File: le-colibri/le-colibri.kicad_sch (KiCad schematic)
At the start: 61 parts, among them SW1 CPG151101S11, SW10 CPG151101S11, SW11 CPG151101S11, SW12 CPG151101S11, SW13 CPG151101S11, SW14 CPG151101S11, SW15 CPG151101S11, SW16 CPG151101S11, SW17 CPG151101S11, SW18 CPG151101S11, SW19 CPG151101S11, SW2 CPG151101S11, SW20 CPG151101S11, SW21 CPG151101S11, SW22 CPG151101S11, SW23 CPG151101S11, SW24 CPG151101S11, SW25 CPG151101S11, SW26 CPG151101S11, SW27 CPG151101S11, SW28 CPG151101S11, SW29 CPG151101S11, SW3 CPG151101S11, SW30 CPG151101S11, SW4 CPG151101S11, SW5 CPG151101S11, SW6 CPG151101S11, SW7 CPG151101S11, SW8 CPG151101S11, SW9 CPG151101S11, U1 Seeeduino Xiao rp2040

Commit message: "first" "release"
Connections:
- net C1: now also U1.4 (P29)
- net C2: now also U1.5 (P6)
- net C3: now also U1.6 (P7)
- net C4: now also U1.7 (P0)
- net C5: now also U1.14 (P1)
- net R1: now also U1.11 (P3)
- net R2: now also U1.12 (P4)
- net R3: now also U1.13 (P2)
- net R4: now also U1.1 (P26)
- net R5: now also U1.2 (P27)
- net R6: now also U1.3 (P28)

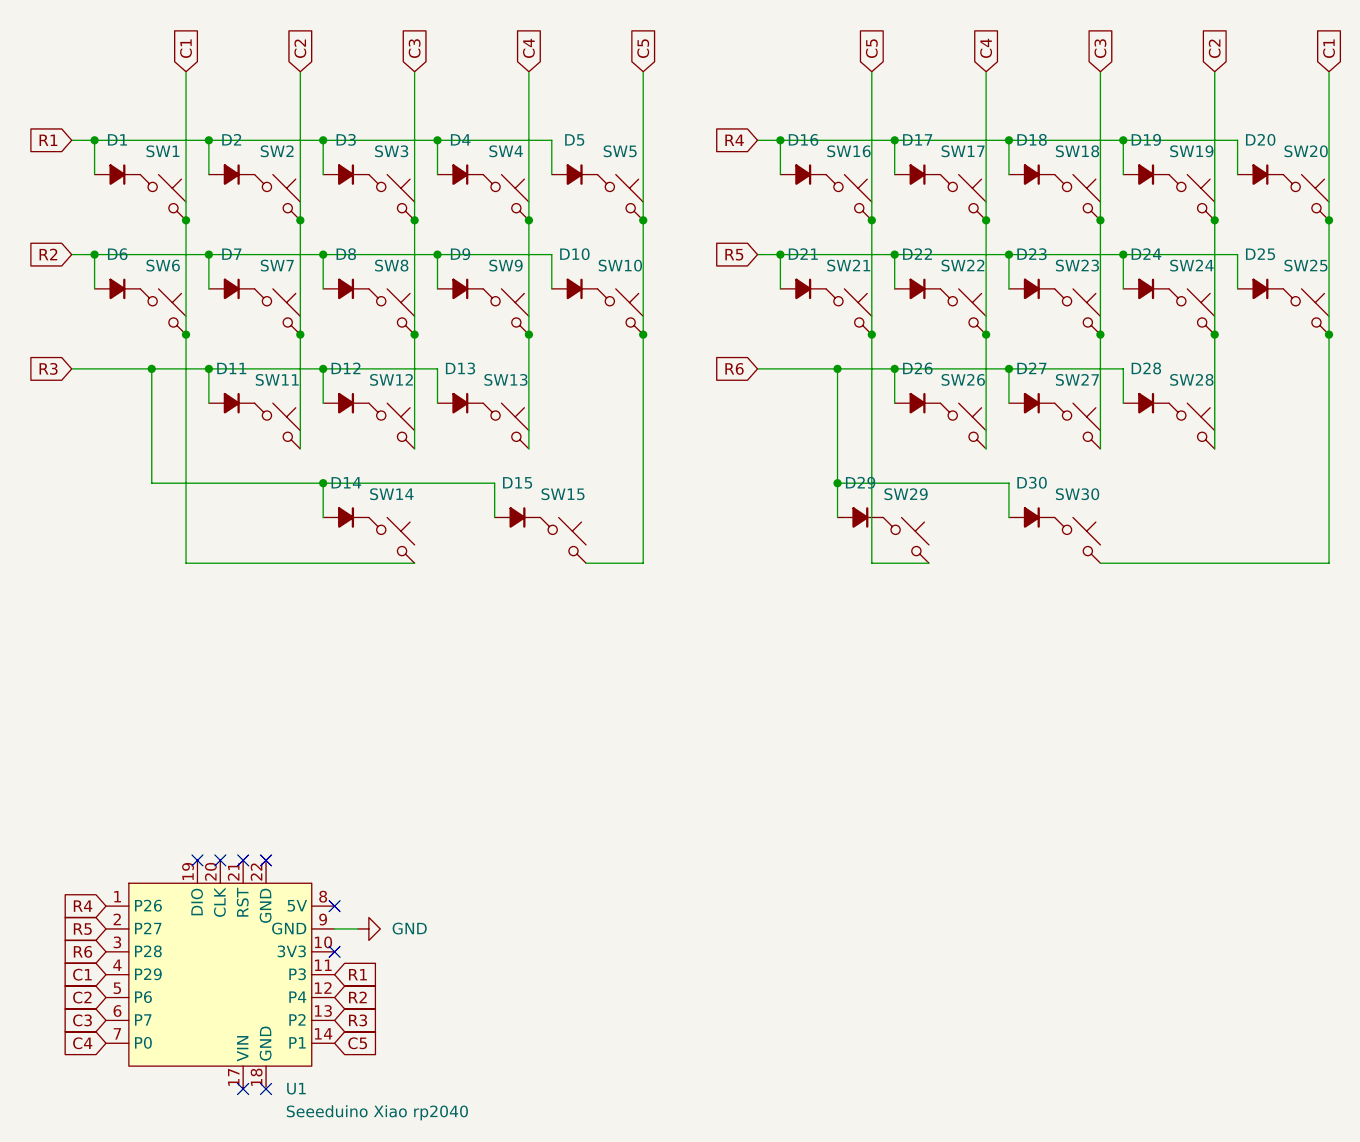
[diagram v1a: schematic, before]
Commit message: added new options for thumbs and pinkie
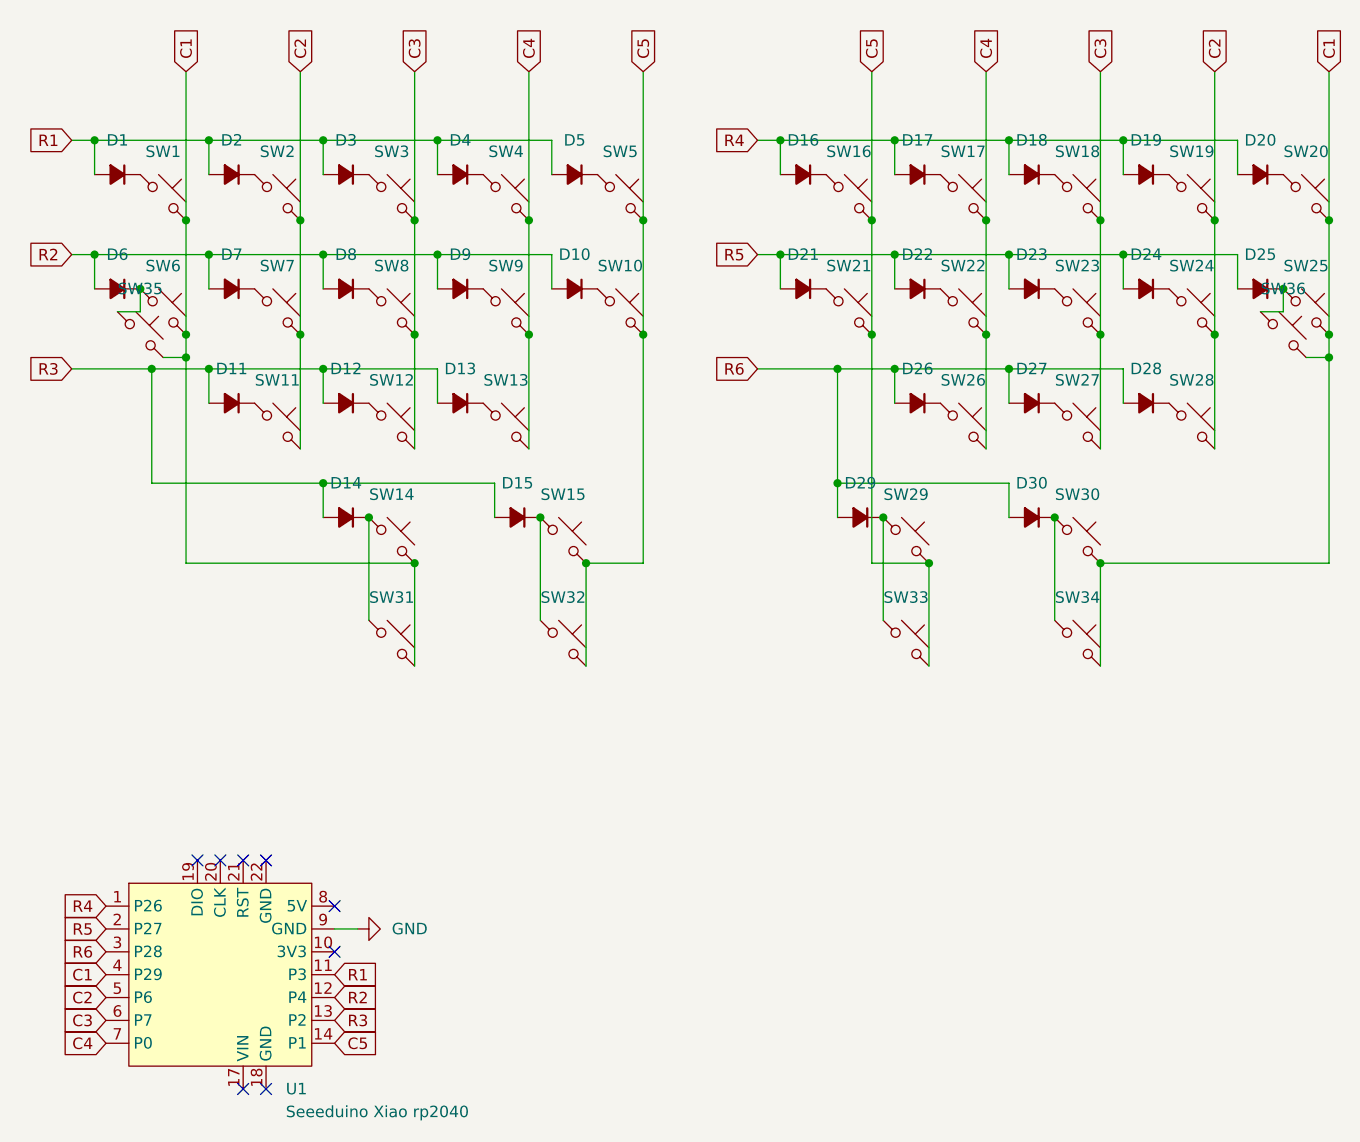
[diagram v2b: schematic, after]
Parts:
- added SW31, SW32, SW33, SW34, SW35, SW36: CPG151101S11, Library:SW_MX_HS_CPG151101S11_1u, symbol Switch:SW_Push_45deg
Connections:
- net C1: now also SW31.2, SW34.2, SW35.2, SW36.2
- net C5: now also SW32.2, SW33.2
- net at D6.1 (K), SW6.1: now also SW35.1
- net at D29.1 (K), SW29.1: now also SW33.1
- net at D15.1 (K), SW15.1: now also SW32.1
- net at D14.1 (K), SW14.1: now also SW31.1
- net at D30.1 (K), SW30.1: now also SW34.1
- net at D25.1 (K), SW25.1: now also SW36.1
